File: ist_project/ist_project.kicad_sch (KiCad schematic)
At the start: 12 parts, among them J0(BOOT0) Conn_01x03, J1(DEBUG) Conn_01x06, SW0 SW_Push, U0 STM32F103RCTx

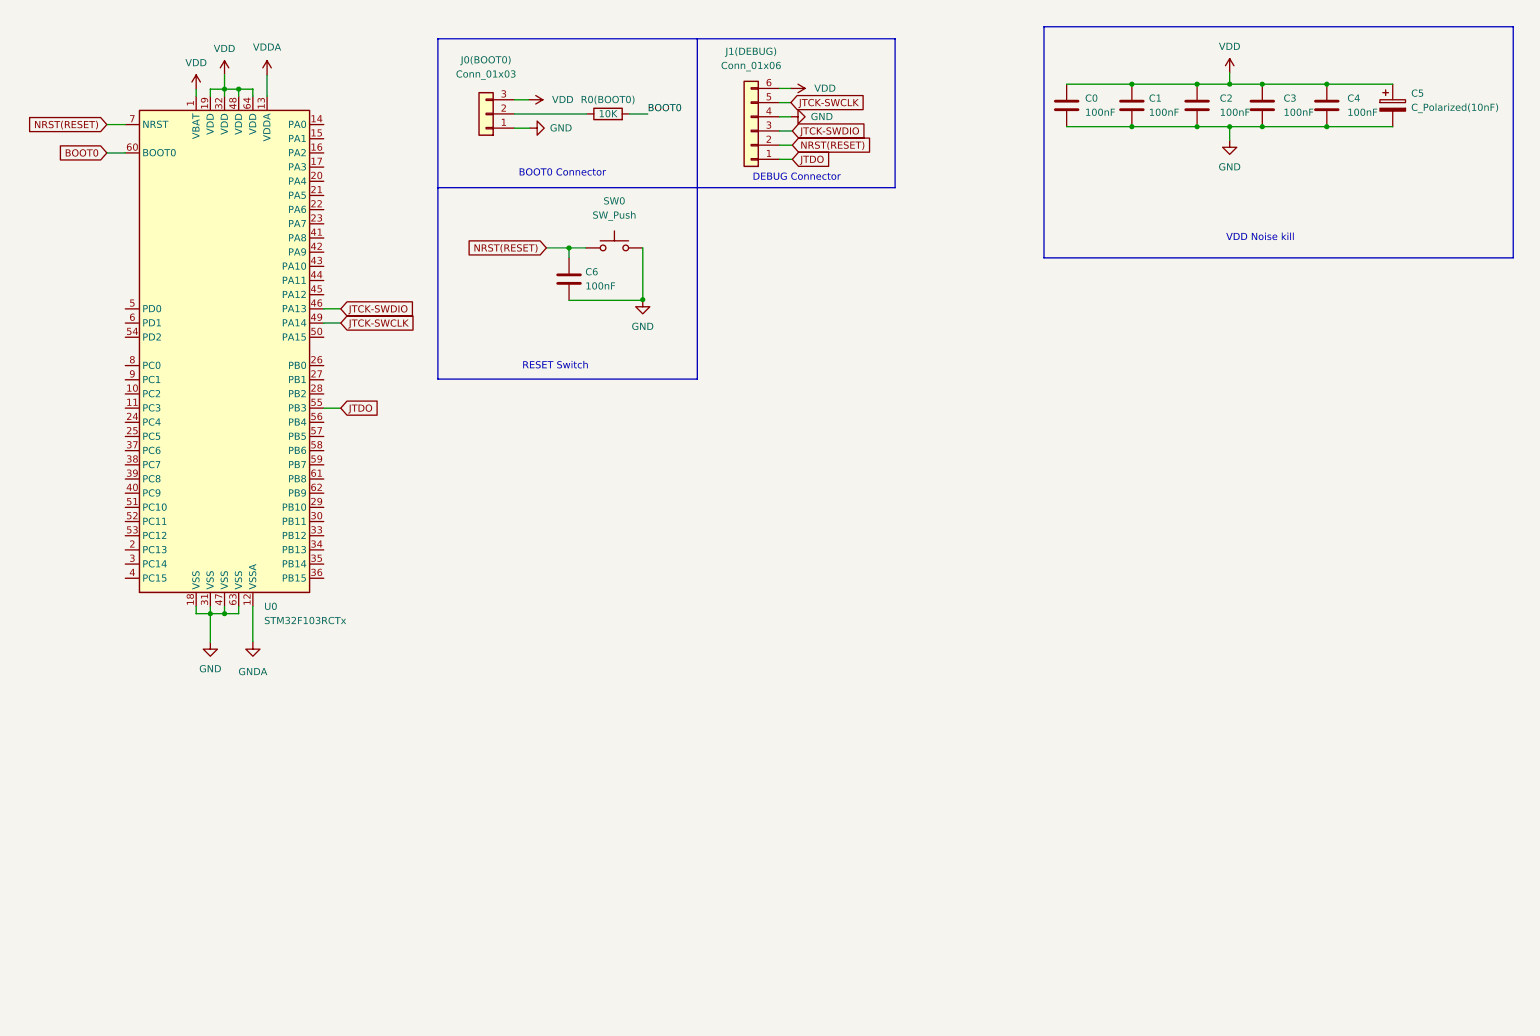
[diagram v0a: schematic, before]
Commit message: Add Pro Micro Library & footprint
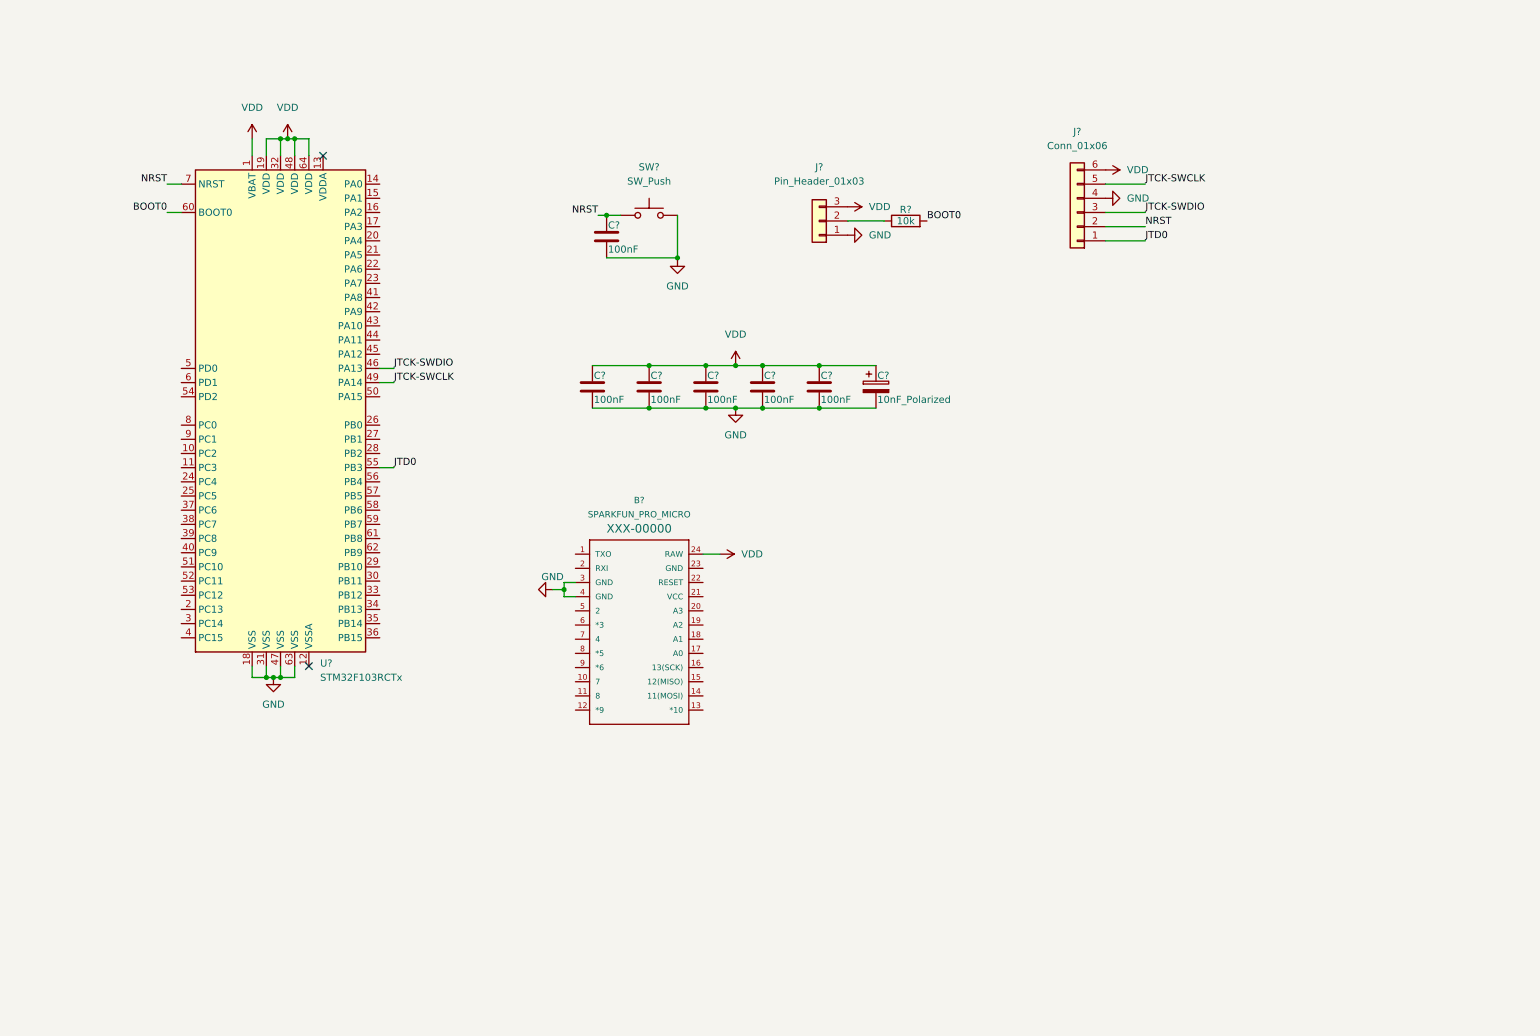
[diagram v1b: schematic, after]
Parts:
- removed C0, C1, C2, C3, C4, C6: 100nF, symbol Device:C
- removed C5: C_Polarized(10nF), symbol Device:C_Polarized
- removed J0(BOOT0): Conn_01x03, symbol Connector_Generic:Conn_01x03
- removed J1(DEBUG): Conn_01x06, symbol Connector_Generic:Conn_01x06
- removed R0(BOOT0): 10K, symbol Device:R
- removed SW0: SW_Push, symbol Switch:SW_Push
- removed U0: STM32F103RCTx, Package_QFP:LQFP-64_10x10mm_P0.5mm, symbol MCU_ST_STM32F1:STM32F103RCTx
- added B?: SPARKFUN_PRO_MICRO, SPARKFUN_PRO_MICRO, symbol SparkFun-Boards:SPARKFUN_PRO_MICRO
- added C? (x6): 100nF, symbol Device:C
- added C?: 10nF_Polarized, symbol Device:C_Polarized
- added J?: Pin_Header_01x03, symbol Connector_Generic:Conn_01x03
- added J?: Conn_01x06, symbol Connector_Generic:Conn_01x06
- added R?: 10k, symbol Device:R
- added SW?: SW_Push, symbol Switch:SW_Push
- added U?: STM32F103RCTx, Package_QFP:LQFP-64_10x10mm_P0.5mm, symbol MCU_ST_STM32F1:STM32F103RCTx
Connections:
- net BOOT0: now also R?.2, U?.60 (BOOT0)
- net GND: now also B?.3 (GND), B?.4 (GND), C?.2, C?.2, C?.2, C?.2, C?.2, C?.2, C?.2, J?.1 (Pin_1), J?.4 (Pin_4), SW?.2, U?.18 (VSS), U?.31 (VSS), U?.47 (VSS), U?.63 (VSS)
- net JTCK-SWCLK: now also J?.5 (Pin_5), U?.49 (PA14)
- net JTCK-SWDIO: now also J?.3 (Pin_3), U?.46 (PA13)
- net VDD: now also B?.24 (RAW), C?.1, C?.1, C?.1, C?.1, C?.1, C?.1, J?.3 (Pin_3), J?.6 (Pin_6), U?.1 (VBAT), U?.19 (VDD), U?.32 (VDD), U?.48 (VDD), U?.64 (VDD)
- new net: J?.2 (Pin_2), R?.1
- new net JTD0: J?.1 (Pin_1), U?.55 (PB3)
- new net NRST: C?.1, J?.2 (Pin_2), SW?.1, U?.7 (NRST)
- no-connect marks 0 -> 2
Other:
- note removed: "BOOT0 Connector"
- note removed: "DEBUG Connector"
- note removed: "RESET Switch"
- note removed: "VDD Noise kill"

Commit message: 회로도 완성 (Atmega32u4 Base)
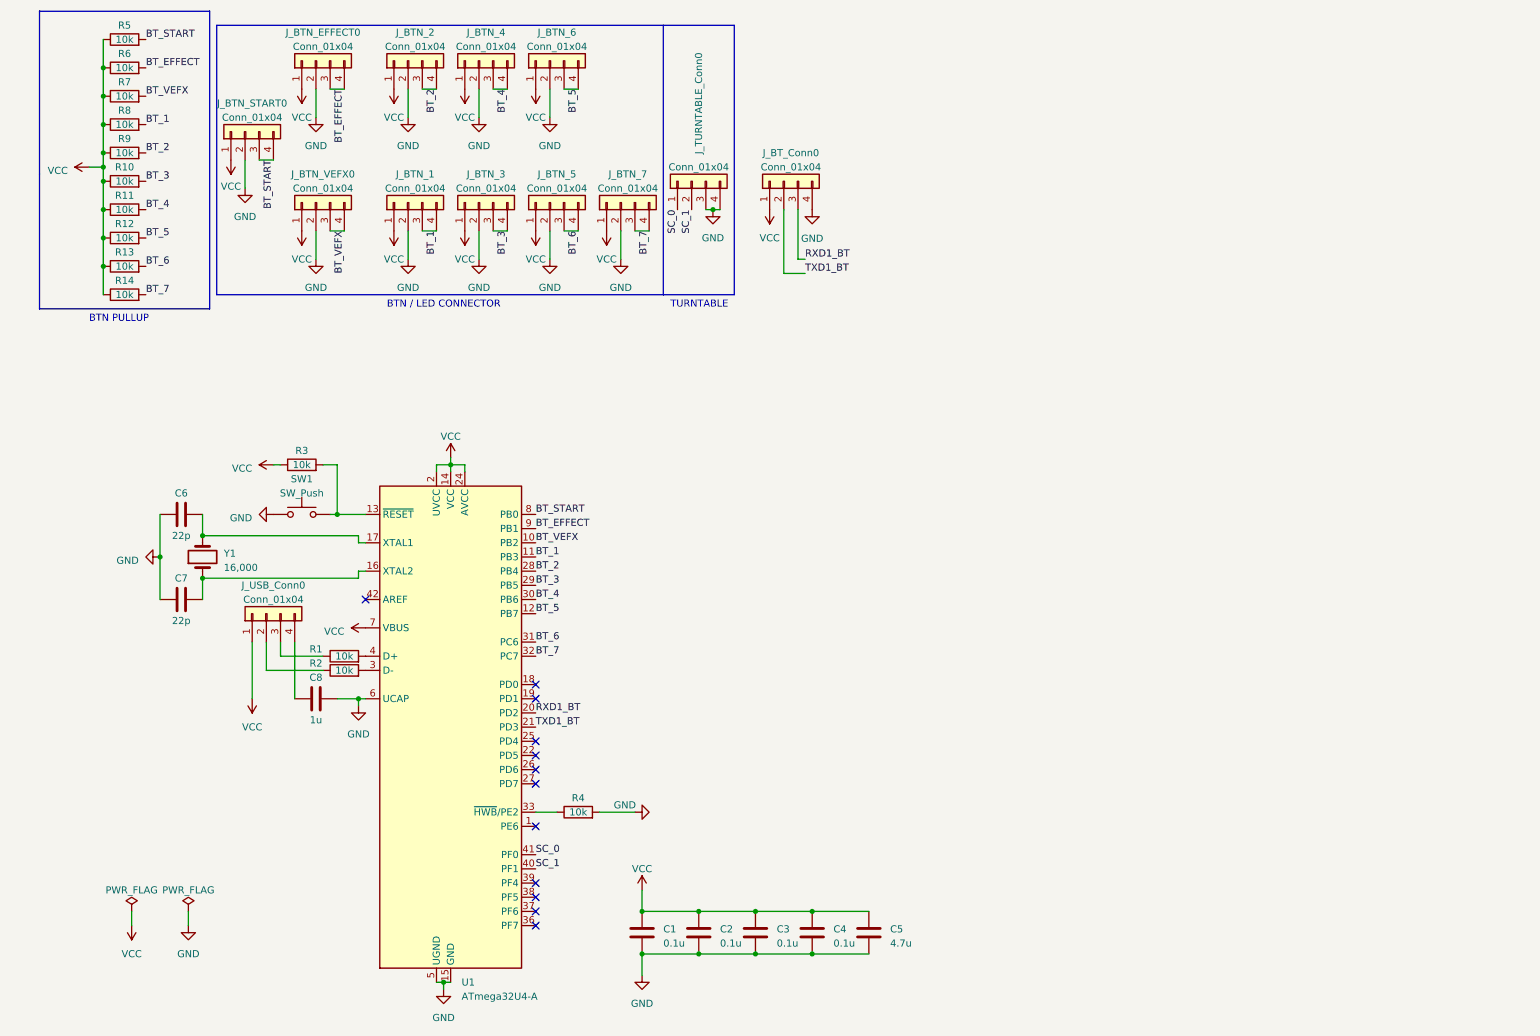
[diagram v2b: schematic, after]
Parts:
- removed B?: SPARKFUN_PRO_MICRO, SPARKFUN_PRO_MICRO, symbol SparkFun-Boards:SPARKFUN_PRO_MICRO
- removed C? (x6): 100nF, symbol Device:C
- removed C?: 10nF_Polarized, symbol Device:C_Polarized
- removed J?: Pin_Header_01x03, symbol Connector_Generic:Conn_01x03
- removed J?: Conn_01x06, symbol Connector_Generic:Conn_01x06
- removed R?: 10k, symbol Device:R
- removed SW?: SW_Push, symbol Switch:SW_Push
- removed U?: STM32F103RCTx, Package_QFP:LQFP-64_10x10mm_P0.5mm, symbol MCU_ST_STM32F1:STM32F103RCTx
- added C1, C2, C3, C4: 0.1u, Capacitor_SMD:C_0805_2012Metric_Pad1.18x1.45mm_HandSolder, symbol Device:C
- added C5: 4.7u, Capacitor_SMD:C_0805_2012Metric_Pad1.18x1.45mm_HandSolder, symbol Device:C
- added C6, C7: 22p, Capacitor_SMD:C_0805_2012Metric_Pad1.18x1.45mm_HandSolder, symbol Device:C
- added C8: 1u, Capacitor_SMD:C_0805_2012Metric_Pad1.18x1.45mm_HandSolder, symbol Device:C
- added J_BTN_1, J_BTN_2, J_BTN_3, J_BTN_4, J_BTN_5, J_BTN_6, J_BTN_7, J_BTN_EFFECT0, J_BTN_START0, J_BTN_VEFX0, J_BT_Conn0, J_TURNTABLE_Conn0, J_USB_Conn0: Conn_01x04, Connector_Molex:Molex_SPOX_5267-04A_1x04_P2.50mm_Vertical, symbol Connector_Generic:Conn_01x04
- added R1, R10, R11, R12, R13, R14, R2, R3, R4, R5, R6, R7, R8, R9: 10k, Resistor_SMD:R_0805_2012Metric_Pad1.20x1.40mm_HandSolder, symbol Device:R
- added SW1: SW_Push, Button_Switch_SMD:SW_Push_1P1T_NO_6x6mm_H9.5mm, symbol Switch:SW_Push
- added U1: ATmega32U4-A, Package_QFP:TQFP-44_10x10mm_P0.8mm, symbol MCU_Microchip_ATmega:ATmega32U4-A
- added Y1: 16,000, Crystal:Crystal_SMD_HC49-SD_HandSoldering, symbol Device:Crystal
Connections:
- net GND: now also C1.2, C2.2, C3.2, C4.2, C5.2, C6.1, C7.2, C8.2, J_BTN_1.2 (Pin_2), J_BTN_2.2 (Pin_2), J_BTN_3.2 (Pin_2), J_BTN_4.2 (Pin_2), J_BTN_5.2 (Pin_2), J_BTN_6.2 (Pin_2), J_BTN_7.2 (Pin_2), J_BTN_EFFECT0.2 (Pin_2), J_BTN_START0.2 (Pin_2), J_BTN_VEFX0.2 (Pin_2), J_BT_Conn0.4 (Pin_4), J_TURNTABLE_Conn0.3 (Pin_3), J_TURNTABLE_Conn0.4 (Pin_4), R4.2, SW1.1, U1.15 (GND), U1.23 (GND), U1.35 (GND), U1.43 (GND), U1.5 (UGND), U1.6 (UCAP)
- new net: J_USB_Conn0.2 (Pin_2), R2.1
- new net: J_USB_Conn0.3 (Pin_3), R1.1
- new net: C8.1, J_USB_Conn0.4 (Pin_4)
- new net: R3.2, SW1.2, U1.13 (~{RESET})
- new net: C7.1, U1.16 (XTAL2), Y1.1
- new net: R2.2, U1.3 (D-)
- new net: R4.1, U1.33 (~{HWB}/PE2)
- new net: C6.2, U1.17 (XTAL1), Y1.2
- new net: R1.2, U1.4 (D+)
- new net BT_1: J_BTN_1.3 (Pin_3), J_BTN_1.4 (Pin_4), R8.2, U1.11 (PB3)
- new net BT_2: J_BTN_2.3 (Pin_3), J_BTN_2.4 (Pin_4), R9.2, U1.28 (PB4)
- new net BT_3: J_BTN_3.3 (Pin_3), J_BTN_3.4 (Pin_4), R10.2, U1.29 (PB5)
- new net BT_4: J_BTN_4.3 (Pin_3), J_BTN_4.4 (Pin_4), R11.2, U1.30 (PB6)
- new net BT_5: J_BTN_6.3 (Pin_3), J_BTN_6.4 (Pin_4), R12.2, U1.12 (PB7)
- new net BT_6: J_BTN_5.3 (Pin_3), J_BTN_5.4 (Pin_4), R13.2, U1.31 (PC6)
- new net BT_7: J_BTN_7.3 (Pin_3), J_BTN_7.4 (Pin_4), R14.2, U1.32 (PC7)
- new net BT_EFFECT: J_BTN_EFFECT0.3 (Pin_3), J_BTN_EFFECT0.4 (Pin_4), R6.2, U1.9 (PB1)
- new net BT_START: J_BTN_START0.3 (Pin_3), J_BTN_START0.4 (Pin_4), R5.2, U1.8 (PB0)
- new net BT_VEFX: J_BTN_VEFX0.3 (Pin_3), J_BTN_VEFX0.4 (Pin_4), R7.2, U1.10 (PB2)
- new net RXD1_BT: J_BT_Conn0.3 (Pin_3), U1.20 (PD2)
- new net SC_0: J_TURNTABLE_Conn0.1 (Pin_1), U1.41 (PF0)
- new net SC_1: J_TURNTABLE_Conn0.2 (Pin_2), U1.40 (PF1)
- new net TXD1_BT: J_BT_Conn0.2 (Pin_2), U1.21 (PD3)
- new net VCC: C1.1, C2.1, C3.1, C4.1, C5.1, J_BTN_1.1 (Pin_1), J_BTN_2.1 (Pin_1), J_BTN_3.1 (Pin_1), J_BTN_4.1 (Pin_1), J_BTN_5.1 (Pin_1), J_BTN_6.1 (Pin_1), J_BTN_7.1 (Pin_1), J_BTN_EFFECT0.1 (Pin_1), J_BTN_START0.1 (Pin_1), J_BTN_VEFX0.1 (Pin_1), J_BT_Conn0.1 (Pin_1), J_USB_Conn0.1 (Pin_1), R10.1, R11.1, R12.1, R13.1, R14.1, R3.1, R5.1, R6.1, R7.1, R8.1, R9.1, U1.14 (VCC), U1.2 (UVCC), U1.24 (AVCC), U1.34 (VCC), U1.44 (AVCC), U1.7 (VBUS)
- no-connect marks 2 -> 12
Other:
- note added: "BTN / LED CONNECTOR"
- note added: "BTN PULLUP"
- note added: "TURNTABLE"

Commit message: 회로도 수정 / pcb 작업중
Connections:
- net BT_5: now also J_BTN_5.3 (Pin_3), J_BTN_5.4 (Pin_4); no longer J_BTN_6.3 (Pin_3), J_BTN_6.4 (Pin_4)
- net BT_6: now also J_BTN_6.3 (Pin_3), J_BTN_6.4 (Pin_4); no longer J_BTN_5.3 (Pin_3), J_BTN_5.4 (Pin_4)
- net GND: now also J_TURNTABLE_Conn0.2 (Pin_2); no longer J_TURNTABLE_Conn0.3 (Pin_3), J_TURNTABLE_Conn0.4 (Pin_4)
- net SC_0: now also J_TURNTABLE_Conn0.3 (Pin_3); no longer J_TURNTABLE_Conn0.1 (Pin_1)
- net SC_1: now also J_TURNTABLE_Conn0.4 (Pin_4); no longer J_TURNTABLE_Conn0.2 (Pin_2)
- net VCC: now also J_TURNTABLE_Conn0.1 (Pin_1)
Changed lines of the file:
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@@
   (junction (at 29.21 58.42) (diameter 0) (color 0 0 0 0)
-  )
-  (junction (at 138.43 48.26) (diameter 0) (color 0 0 0 0)
   )
   (junction (at 29.21 27.94) (diameter 0) (color 0 0 0 0)
@@
     (stroke (width 0) (type default))
   )
+  (wire (pts (xy 134.62 52.07) (xy 134.62 48.26))
+    (stroke (width 0) (type default))
+  )
   (wire (pts (xy 71.12 93.98) (xy 71.12 102.87))
     (stroke (width 0) (type default))
@@
     (stroke (width 0) (type default))
   )
-  (wire (pts (xy 138.43 48.26) (xy 139.7 48.26))
-    (stroke (width 0) (type default))
-  )
   (wire (pts (xy 90.17 186.69) (xy 91.44 186.69))
     (stroke (width 0) (type default))
@@
     (stroke (width 0) (type default))
   )
-  (wire (pts (xy 137.16 48.26) (xy 138.43 48.26))
-    (stroke (width 0) (type default))
-  )
   (wire (pts (xy 121.92 52.07) (xy 121.92 57.15))
     (stroke (width 0) (type default))
@@
     (effects (font (size 1.27 1.27)) (justify left bottom))
   )
-  (label "SC_0" (at 132.08 48.26 270) (fields_autoplaced)
-    (effects (font (size 1.27 1.27)) (justify right bottom))
-  )
   (label "TXD1_BT" (at 154.94 59.69 0) (fields_autoplaced)
     (effects (font (size 1.27 1.27)) (justify left bottom))
-  )
-  (label "BT_6" (at 114.3 52.07 270) (fields_autoplaced)
-    (effects (font (size 1.27 1.27)) (justify right bottom))
   )
   (label "BT_6" (at 106.68 125.73 0) (fields_autoplaced)
@@
     (effects (font (size 1.27 1.27)) (justify left bottom))
   )
+  (label "SC_0" (at 137.16 48.26 270) (fields_autoplaced)
+    (effects (font (size 1.27 1.27)) (justify right bottom))
+  )
   (label "BT_4" (at 106.68 118.11 0) (fields_autoplaced)
     (effects (font (size 1.27 1.27)) (justify left bottom))
@@
     (effects (font (size 1.27 1.27)) (justify right bottom))
   )
-  (label "BT_5" (at 114.3 26.67 270) (fields_autoplaced)
-    (effects (font (size 1.27 1.27)) (justify right bottom))
-  )
   (label "BT_3" (at 106.68 115.57 0) (fields_autoplaced)
     (effects (font (size 1.27 1.27)) (justify left bottom))
@@
     (effects (font (size 1.27 1.27)) (justify left bottom))
   )
+  (label "BT_6" (at 114.2315 26.67 270) (fields_autoplaced)
+    (effects (font (size 1.27 1.27)) (justify right bottom))
+  )
   (label "BT_2" (at 36.83 38.1 0) (fields_autoplaced)
     (effects (font (size 1.27 1.27)) (justify left bottom))
@@
     (effects (font (size 1.27 1.27)) (justify left bottom))
   )
-  (label "SC_1" (at 134.62 48.26 270) (fields_autoplaced)
+  (label "BT_5" (at 114.3 52.07 270) (fields_autoplaced)
     (effects (font (size 1.27 1.27)) (justify right bottom))
   )
   (label "BT_4" (at 101.6 26.67 270) (fields_autoplaced)
+    (effects (font (size 1.27 1.27)) (justify right bottom))
+  )
+  (label "SC_1" (at 139.7 48.26 270) (fields_autoplaced)
     (effects (font (size 1.27 1.27)) (justify right bottom))
   )
@@
     )
   )
+  (symbol (lib_id "power:VCC") (at 132.08 48.26 180) (unit 1)
+    (in_bom yes) (on_board yes) (dnp no) (fields_autoplaced)
+    (property "Reference" "#PWR038" (at 132.08 44.45 0)
+      (effects (font (size 1.27 1.27)) hide)
+    )
+    (property "Value" "VCC" (at 132.08 53.34 0)
+      (effects (font (size 1.27 1.27)))
+    )
+    (property "Footprint" "" (at 132.08 48.26 0)
+      (effects (font (size 1.27 1.27)) hide)
+    )
+    (property "Datasheet" "" (at 132.08 48.26 0)
+      (effects (font (size 1.27 1.27)) hide)
+    )
+    (pin "1")
+    (instances
+      (project "ist_project"
+        (path "/a35c2728-7b0f-4f87-b127-69e8487497c2"
+          (reference "#PWR038") (unit 1)
+        )
+      )
+    )
+  )
   (symbol (lib_id "power:GND") (at 124.46 156.21 90) (unit 1)
     (in_bom yes) (on_board yes) (dnp no)
@@
     )
   )
-  (symbol (lib_id "power:GND") (at 138.43 48.26 0) (unit 1)
-    (in_bom yes) (on_board yes) (dnp no) (fields_autoplaced)
-    (property "Reference" "#PWR033" (at 138.43 54.61 0)
-      (effects (font (size 1.27 1.27)) hide)
-    )
-    (property "Value" "GND" (at 138.43 53.34 0)
-      (effects (font (size 1.27 1.27)))
-    )
-    (property "Footprint" "" (at 138.43 48.26 0)
-      (effects (font (size 1.27 1.27)) hide)
-    )
-    (property "Datasheet" "" (at 138.43 48.26 0)
-      (effects (font (size 1.27 1.27)) hide)
-    )
+  (symbol (lib_id "power:GND") (at 134.62 52.07 0) (unit 1)
+    (in_bom yes) (on_board yes) (dnp no) (fields_autoplaced)
+    (property "Reference" "#PWR033" (at 134.62 58.42 0)
+      (effects (font (size 1.27 1.27)) hide)
+    )
+    (property "Value" "GND" (at 134.62 57.15 0)
+      (effects (font (size 1.27 1.27)))
+    )
+    (property "Footprint" "" (at 134.62 52.07 0)
+      (effects (font (size 1.27 1.27)) hide)
+    )
+    (property "Datasheet" "" (at 134.62 52.07 0)
+      (effects (font (size 1.27 1.27)) hide)
+    )
